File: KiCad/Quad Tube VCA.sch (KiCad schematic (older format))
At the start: 226 parts, among them IC1 TL072, IC10 TL072, IC2 LM358, IC3 TL072, IC4 LM358, IC5 TL072, IC6 LM358, IC7 TL072, IC8 LM358, IC9 TL072

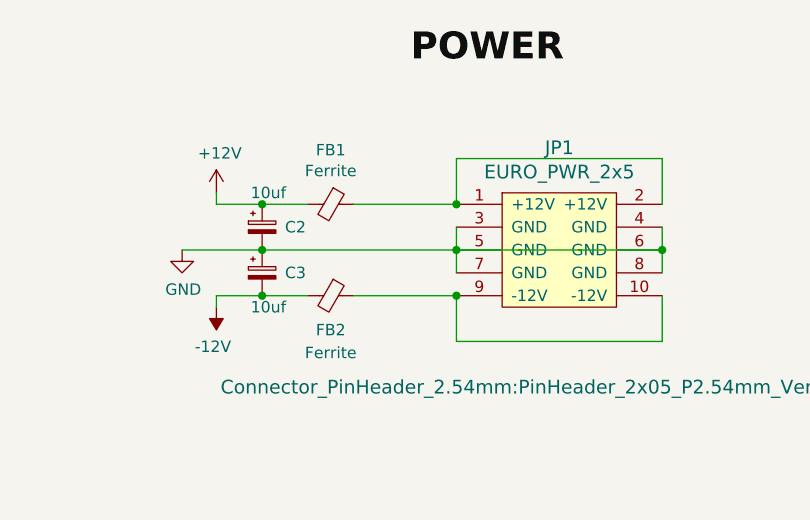
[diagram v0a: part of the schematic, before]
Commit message: adds reverse power protection diodes
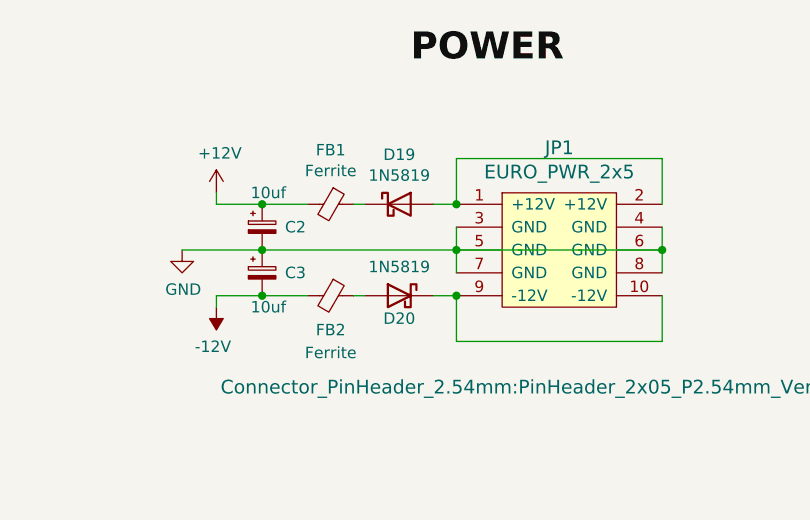
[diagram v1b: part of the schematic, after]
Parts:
- added D19, D20: 1N5819, Diode_SMD:D_SOD-123, symbol Diode:1N5819
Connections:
- net at JP1.1 (+12V), JP1.2 (+12V): now also D19.2 (A); no longer FB1.1
- net at JP1.10 (-12V), JP1.9 (-12V): now also D20.1 (K); no longer FB2.1
- new net: D20.2 (A), FB2.1
- new net: D19.1 (K), FB1.1
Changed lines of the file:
@@
 $EndComp
 Wire Wire Line
-	14150 2000 14600 2000
-Wire Wire Line
-	14150 2400 14600 2400
+	14150 2400 14200 2400
 Wire Wire Line
 	13750 2200 14600 2200
@@
 	1    0    0    1
 $EndComp
+Wire Wire Line
+	14150 2000 14200 2000
+Wire Wire Line
+	14500 2000 14600 2000
+$Comp
+L Diode:1N5819 D19
+U 1 1 61F82084
+P 14350 2000
+F 0 "D19" H 14350 2217 50  0000 C CNN
+F 1 "1N5819" H 14350 2126 50  0000 C CNN
+F 2 "Diode_SMD:D_SOD-123" H 14350 1825 50  0001 C CNN
+F 3 "http://www.vishay.com/docs/88525/1n5817.pdf" H 14350 2000 50  0001 C CNN
+	1    14350 2000
+	1    0    0    -1
+$EndComp
+$Comp
+L Diode:1N5819 D20
+U 1 1 61F9AC47
+P 14350 2400
+F 0 "D20" H 14350 2300 50  0000 C CNN
+F 1 "1N5819" H 14350 2526 50  0000 C CNN
+F 2 "Diode_SMD:D_SOD-123" H 14350 2225 50  0001 C CNN
+F 3 "http://www.vishay.com/docs/88525/1n5817.pdf" H 14350 2400 50  0001 C CNN
+	1    14350 2400
+	-1   0    0    -1
+$EndComp
+Wire Wire Line
+	14500 2400 14600 2400
 $EndSCHEMATC

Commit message: removes leds from cathode/signal path
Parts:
- removed D10, D13, D14, D17, D18, D5, D6, D9: 1n4148, Diode_SMD:D_SOD-323_HandSoldering, symbol Device:D_Small_ALT
- added R92, R93, R94, R95: 750R, Resistor_SMD:R_1206_3216Metric, symbol Device:R_US
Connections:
- net +12V: now also D11.2 (A), D12.2 (A), D15.2 (A), D16.2 (A), D3.2 (A), D4.2 (A), D7.2 (A), D8.2 (A)
- net GND: now also R11.1, R13.2, R31.1, R33.2, R51.1, R53.2, R71.1, R73.2, R92.2, R93.2, R94.2, R95.2; no longer D11.2 (A), D12.2 (A), D15.2 (A), D16.2 (A), D3.2 (A), D4.2 (A), D7.2 (A), D8.2 (A)
- new net: R92.1, V1.1
- new net: R93.1, V2.1
- new net: R94.1, V3.1
- new net: R95.1, V4.1
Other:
- moved on the sheet: D11, D12, D15, D16, D3, D4, D7, D8, R11, R13, R31, R33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

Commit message: updates annotations - need to regen BOM
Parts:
- renumbered C2 to C1, C51 to C10, C10 to C11, C11 to C12, C52 to C13, C12 to C14, C13 to C15, C14 to C16, C15 to C17, C16 to C18, C17 to C19, C3 to C2, C18 to C20, C19 to C21, C20 to C24, C21 to C25, C24 to C26, C25 to C27, C26 to C28, C27 to C29, C1 to C3, C28 to C30, C29 to C31, C30 to C32, C31 to C33, C32 to C34, C33 to C35, C53 to C36, C34 to C37, C35 to C38, C54 to C39, C36 to C40, C37 to C41, C38 to C42, C39 to C43, C40 to C44, C41 to C45, C42 to C46, C43 to C47, C44 to C48, C45 to C49, C46 to C50, C47 to C51, C48 to C52, C49 to C53, C50 to C54, D19 to D1, D16 to D10, D20 to D2, D7 to D5, D8 to D6, D11 to D7, D12 to D8, D15 to D9, IC8 to IC10, IC9 to IC2, IC2 to IC3, IC3 to IC4, IC4 to IC5, IC5 to IC6, IC10 to IC7, IC6 to IC8, IC7 to IC9, R8 to R10, R9 to R11, R10 to R12, R92 to R13, R12 to R14, R11 to R15, R13 to R16, R14 to R17, R15 to R18, R16 to R19, R17 to R20, R18 to R21, R19 to R22, R20 to R23, R21 to R24, R22 to R25, R23 to R26, R24 to R27, R25 to R28, R26 to R29, R85 to R30, R89 to R31, R27 to R32, R28 to R33, R82 to R34, R29 to R35, R30 to R36, R93 to R37, R31 to R38, R32 to R39, R33 to R40, R34 to R41, R35 to R42, R36 to R43, R37 to R44, R38 to R45, R39 to R46, R40 to R47, R41 to R48, R42 to R49, R43 to R50, R44 to R51, R45 to R52, R46 to R53, R86 to R54, R90 to R55, R47 to R56, R48 to R57, R83 to R58, R49 to R59, R50 to R60, R94 to R61, R52 to R62, R51 to R63, R54 to R64, R55 to R65, R53 to R66, R56 to R67, R57 to R68, R58 to R69, R88 to R7, R59 to R70, R60 to R71, R61 to R72, R62 to R73, R63 to R74, R64 to R75, R65 to R76, R66 to R77, R91 to R78, R87 to R79, R7 to R8, R67 to R80, R84 to R81, R68 to R82, R69 to R83, R70 to R84, R95 to R85, R72 to R86, R71 to R87, R74 to R88, R73 to R89, R81 to R9, R75 to R90, R76 to R91, R77 to R92, R78 to R93, R79 to R94, R80 to R95

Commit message: adds inverting buffers, new layout
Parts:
- added C55, C56, C57, C58: 100nf, Capacitor_SMD:C_0603_1608Metric, symbol Device:C_Small
- added IC11, IC12: TL072, Package_SO:SOIC-8_3.9x4.9mm_P1.27mm, symbol Amplifier_Operational:TL072
- added R100, R101, R96, R97, R98, R99: 100k, Resistor_SMD:R_0603_1608Metric, symbol Device:R_Small_US
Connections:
- net +12V: now also C55.1, C57.1, IC11.8 (V+), IC12.8 (V+)
- net -12V: now also C56.2, C58.2, IC11.4 (V-), IC12.4 (V-)
- net GND: now also C55.2, C56.1, C57.2, C58.1, IC11.3 (+), IC11.5 (+), IC12.3 (+), IC12.5 (+)
- net at J_OUT1.2: now also R97.2; no longer R30.2
- net at J_OUT2.2: now also R99.2; no longer R54.2
- net at J_OUT3.2: now also R101.2; no longer R79.2
- new net: IC11.1, R30.2, R96.1
- new net: IC11.2 (-), R96.2, R97.1
- new net: IC11.6 (-), R98.2, R99.1
- new net: IC11.7, R54.2, R98.1
- new net: IC12.1, R100.1, R79.2
- new net: IC12.2 (-), R100.2, R101.1
- new net: IC12.6 (-), IC12.7
